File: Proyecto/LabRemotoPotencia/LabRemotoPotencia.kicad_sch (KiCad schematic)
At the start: 17 parts

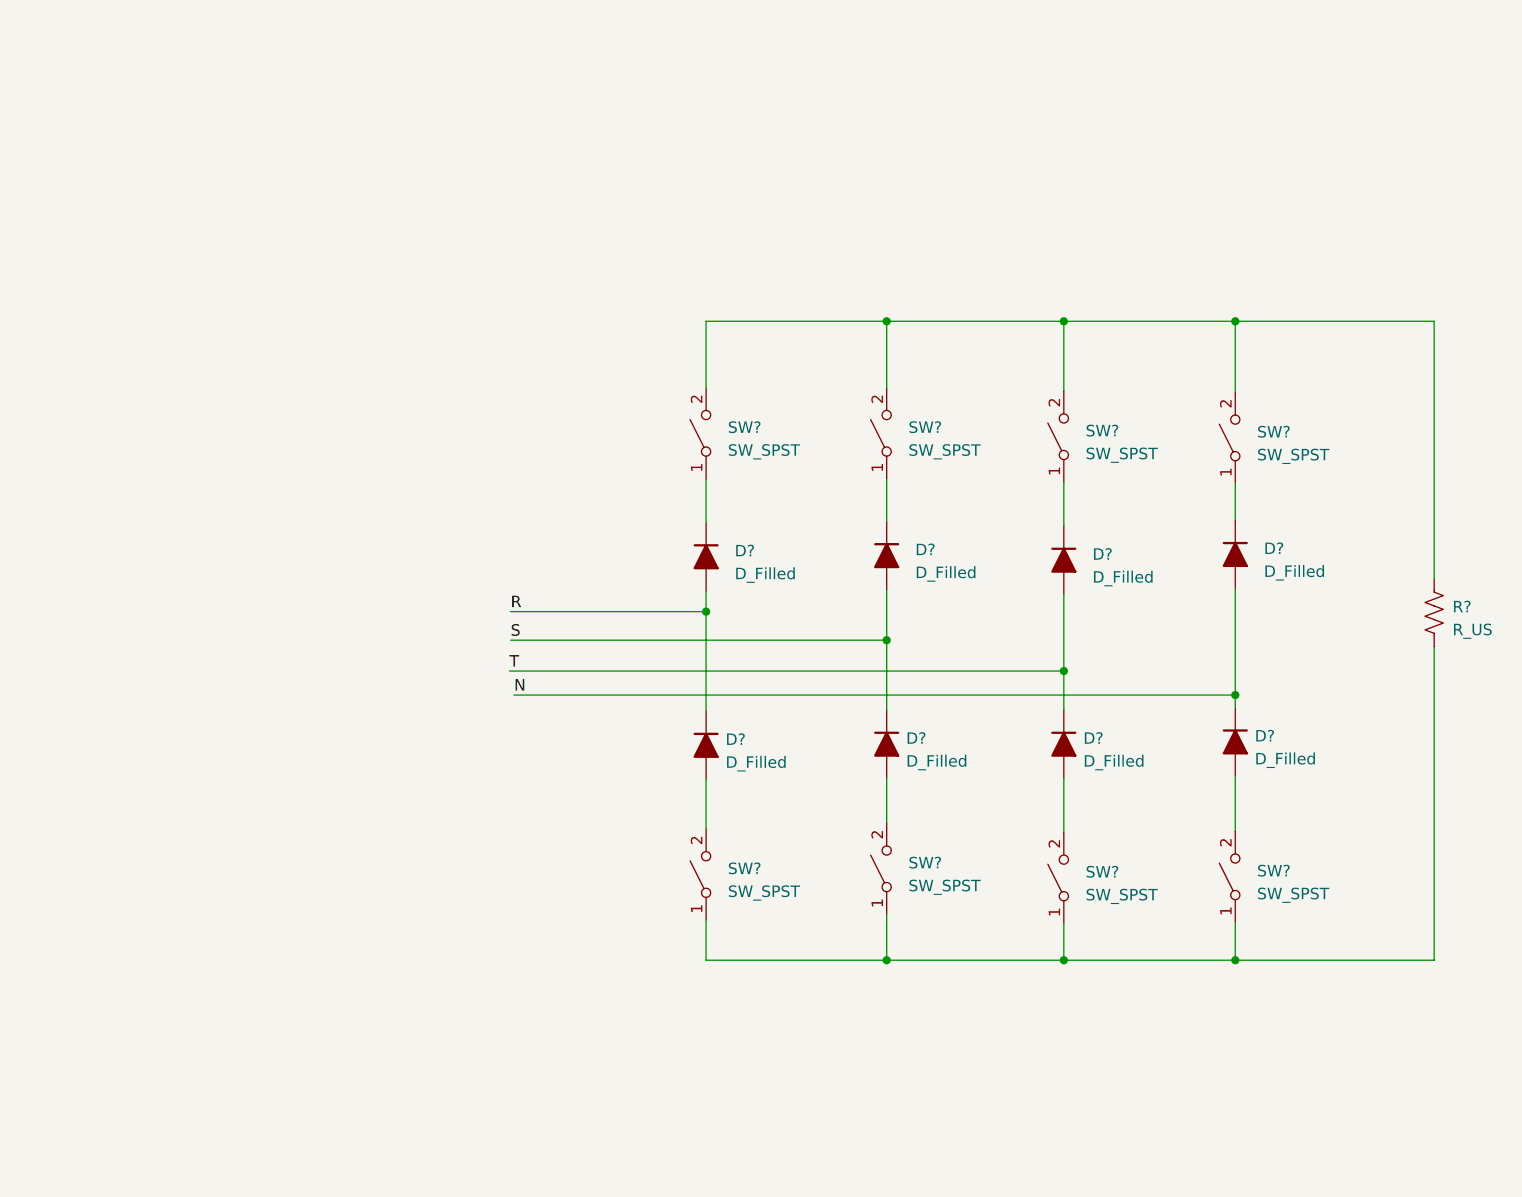
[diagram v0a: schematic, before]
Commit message: 2022-4-15 Se añade la simulacion correspondiente a generador de onda cuadrada de 50Hz implementado con un LM555
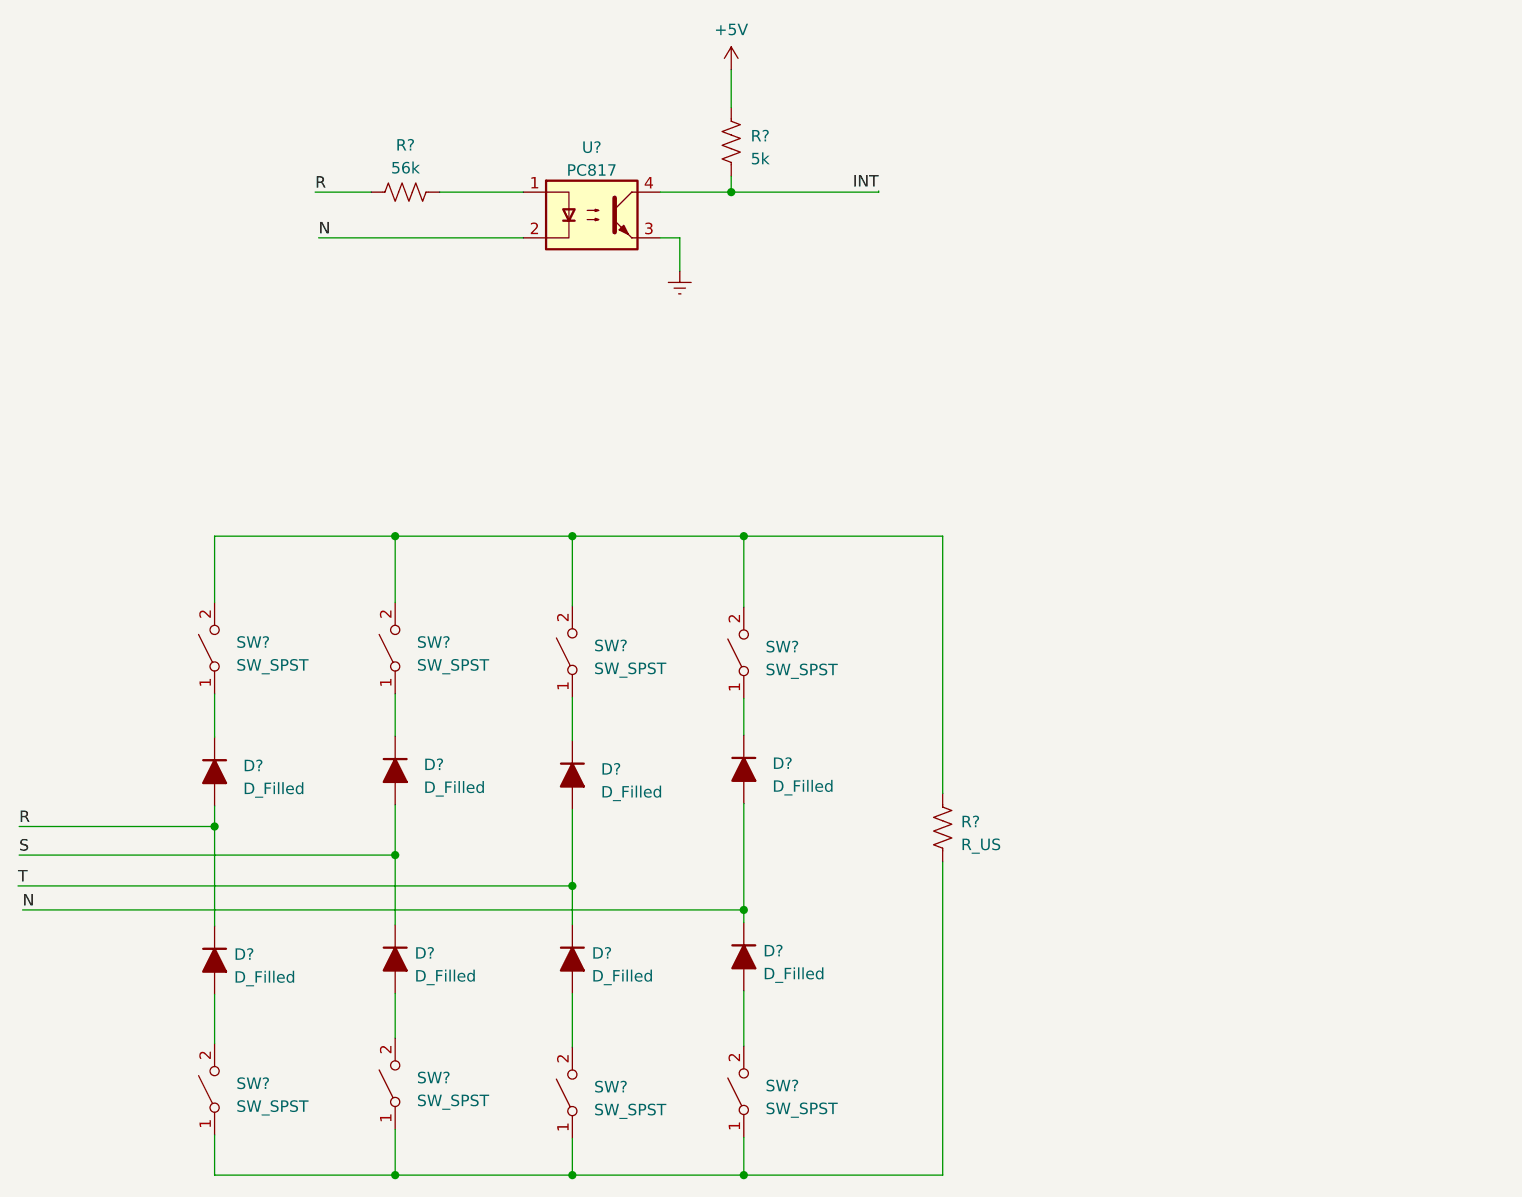
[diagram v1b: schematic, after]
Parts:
- added R?: 5k, symbol Device:R_US
- added R?: 56k, symbol Device:R_US
- added U?: PC817, Package_DIP:DIP-4_W7.62mm, symbol Isolator:PC817
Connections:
- net N: now also U?.2
- net R: now also R?.1
- new net: R?.2, U?.1
- new net +5V: R?.2
- new net Earth: U?.3
- new net INT: R?.1, U?.4
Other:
- moved on the sheet: D?, R?, SW?
